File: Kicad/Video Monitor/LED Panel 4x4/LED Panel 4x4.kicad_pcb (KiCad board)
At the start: 2 copper layers, 20.1 x 20.1 mm, 34 parts, among them IC2 74VHC273FT, IC3 74VHC273FT

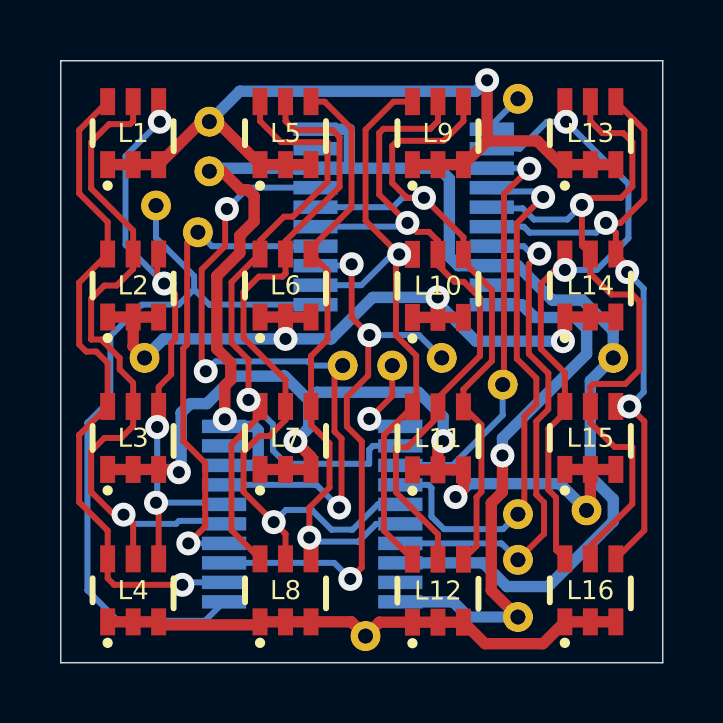
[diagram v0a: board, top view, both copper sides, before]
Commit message: LED Address attempted.
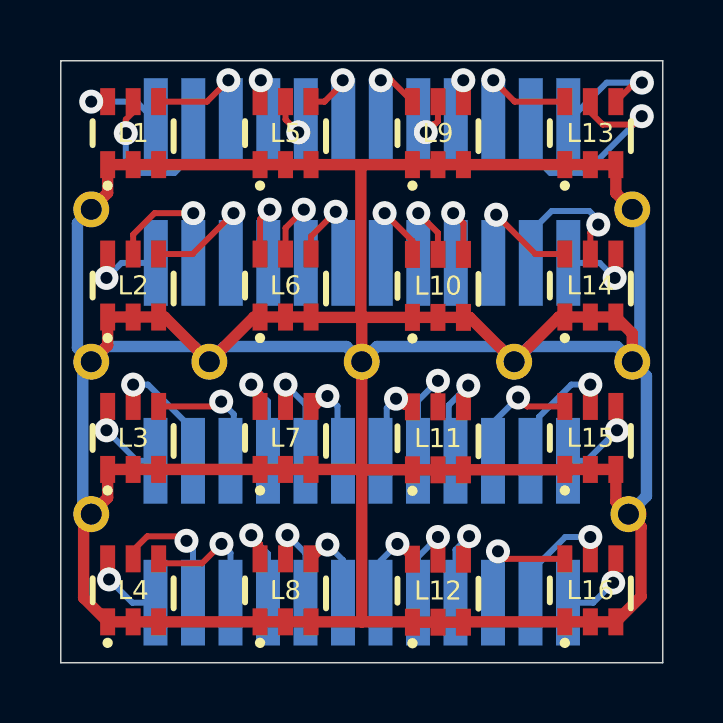
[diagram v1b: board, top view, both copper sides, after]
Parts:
- removed IC2, IC3: 74VHC273FT, SamacSys_Parts:SOP65P640X110-20N
- removed TP10, TP11, TP12, TP13, TP14, TP15, TP16: TestPoint, SamacSys_Parts:Point_D1.0mm_Drill0.5mm
- added J1: 504187-2470, SamacSys_Parts:5041872470, B.Cu at (125.3, 69.9)
- added J2: 504187-2470, SamacSys_Parts:5041872470, B.Cu at (125.3, 80.6)
- moved TP1 15.7 mm to (116.3, 75.2)
- moved TP3 14.4 mm to (116.3, 80.3)
- moved TP4 10.7 mm to (134.2, 80.3)
- moved TP9 8.76 mm to (130.3, 75.2)
- moved TP7 8.61 mm to (125.3, 75.2)
- moved TP6 8.05 mm to (134.3, 70.2)
- moved TP2 6.35 mm to (134.3, 75.2)
- moved TP8 6.10 mm to (120.2, 75.2)
- moved TP5 3.64 mm to (116.3, 70.2)
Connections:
- L1 pad C1: /G1 -> /GND
- L1 pad C2: /G1 -> /GND
- L1 pad C3: /G1 -> /GND
- L10 pad A1: /Q6 -> /Q18
- L10 pad A2: /Q7 -> /Q19
- L10 pad A3: /Q8 -> /Q20
- L10 pad C1: /G2 -> /GND
- L10 pad C2: /G2 -> /GND
- L10 pad C3: /G2 -> /GND
- L11 pad A1: /Q6 -> /Q30
- L11 pad A2: /Q7 -> /Q31
- L11 pad A3: /Q8 -> /Q32
- L11 pad C1: /G3 -> /GND
- L11 pad C2: /G3 -> /GND
- L11 pad C3: /G3 -> /GND
- L12 pad A1: /Q6 -> /Q42
- L12 pad A2: /Q7 -> /Q43
- L12 pad A3: /Q8 -> /Q44
- L12 pad C1: /G4 -> /GND
- L12 pad C2: /G4 -> /GND
- L12 pad C3: /G4 -> /GND
- L13 pad C1: /G1 -> /GND
- L13 pad C2: /G1 -> /GND
- L13 pad C3: /G1 -> /GND
- L14 pad A1: /Q9 -> /Q21
- L14 pad A2: /Q10 -> /Q22
- L14 pad A3: /Q11 -> /Q23
- L14 pad C1: /G2 -> /GND
- L14 pad C2: /G2 -> /GND
- L14 pad C3: /G2 -> /GND
- L15 pad A1: /Q9 -> /Q33
- L15 pad A2: /Q10 -> /Q34
- L15 pad A3: /Q11 -> /Q35
- L15 pad C1: /G3 -> /GND
- L15 pad C2: /G3 -> /GND
- L15 pad C3: /G3 -> /GND
- L16 pad A1: /Q9 -> /Q45
- L16 pad A2: /Q10 -> /Q46
- L16 pad A3: /Q11 -> /Q47
- L16 pad C1: /G4 -> /GND
- L16 pad C2: /G4 -> /GND
- L16 pad C3: /G4 -> /GND
- L2 pad A1: /Q0 -> /Q12
- L2 pad A2: /Q1 -> /Q13
- L2 pad A3: /Q2 -> /Q14
- L2 pad C1: /G2 -> /GND
- L2 pad C2: /G2 -> /GND
- L2 pad C3: /G2 -> /GND
- L3 pad A1: /Q0 -> /Q24
- L3 pad A2: /Q1 -> /Q25
- L3 pad A3: /Q2 -> /Q26
- L3 pad C1: /G3 -> /GND
- L3 pad C2: /G3 -> /GND
- L3 pad C3: /G3 -> /GND
- L4 pad A1: /Q0 -> /Q36
- L4 pad A2: /Q1 -> /Q37
- L4 pad A3: /Q2 -> /Q38
- L4 pad C1: /G4 -> /GND
- L4 pad C2: /G4 -> /GND
- L4 pad C3: /G4 -> /GND
- L5 pad C1: /G1 -> /GND
- L5 pad C2: /G1 -> /GND
- L5 pad C3: /G1 -> /GND
- L6 pad A1: /Q3 -> /Q15
- L6 pad A2: /Q4 -> /Q16
- L6 pad A3: /Q5 -> /Q17
- L6 pad C1: /G2 -> /GND
- L6 pad C2: /G2 -> /GND
- L6 pad C3: /G2 -> /GND
- L7 pad A1: /Q3 -> /Q27
- L7 pad A2: /Q4 -> /Q28
- L7 pad A3: /Q5 -> /Q29
- L7 pad C1: /G3 -> /GND
- L7 pad C2: /G3 -> /GND
- L7 pad C3: /G3 -> /GND
- L8 pad A1: /Q3 -> /Q39
- L8 pad A2: /Q4 -> /Q40
- L8 pad A3: /Q5 -> /Q41
- L8 pad C1: /G4 -> /GND
- L8 pad C2: /G4 -> /GND
- L8 pad C3: /G4 -> /GND
- L9 pad C1: /G1 -> /GND
- L9 pad C2: /G1 -> /GND
- L9 pad C3: /G1 -> /GND
- TP1 pad 1: /D5 -> /GND
- TP2 pad 1: /D4 -> /GND
- TP3 pad 1: /D3 -> /GND
- TP4 pad 1: /D2 -> /GND
- TP5 pad 1: /D1 -> /GND
- TP6 pad 1: /D0 -> /GND
- TP7 pad 1: /~{Reset} -> /GND
- TP8 pad 1: /~{Y0} -> /GND
- TP9 pad 1: /~{Y1} -> /GND
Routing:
- net /GND: track 49.8 -> 142.9 mm, vias 1 -> 0
- net /G3: track 31.3 -> 0.00 mm, vias 4 -> 0
- net /G1: track 26.7 -> 0.00 mm, vias 1 -> 0
- net /G2: track 26.0 -> 0.00 mm, vias 3 -> 0
- net /~{Reset}: track 25.0 -> 0.00 mm
- net /Q3: track 26.5 -> 1.83 mm
- net /Q4: track 25.5 -> 1.20 mm
- net /D2: track 22.6 -> 0.00 mm, vias 3 -> 0
- net /Q7: track 23.2 -> 1.21 mm
- net /Q8: track 23.3 -> 1.82 mm
- net /D0: track 19.8 -> 0.00 mm, vias 3 -> 0
- net /Q0: track 22.5 -> 2.97 mm
- net /Q1: track 23.5 -> 4.46 mm
- net /Q6: track 21.7 -> 2.71 mm
- net /3.3V: track 18.9 -> 0.00 mm, vias 1 -> 0
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
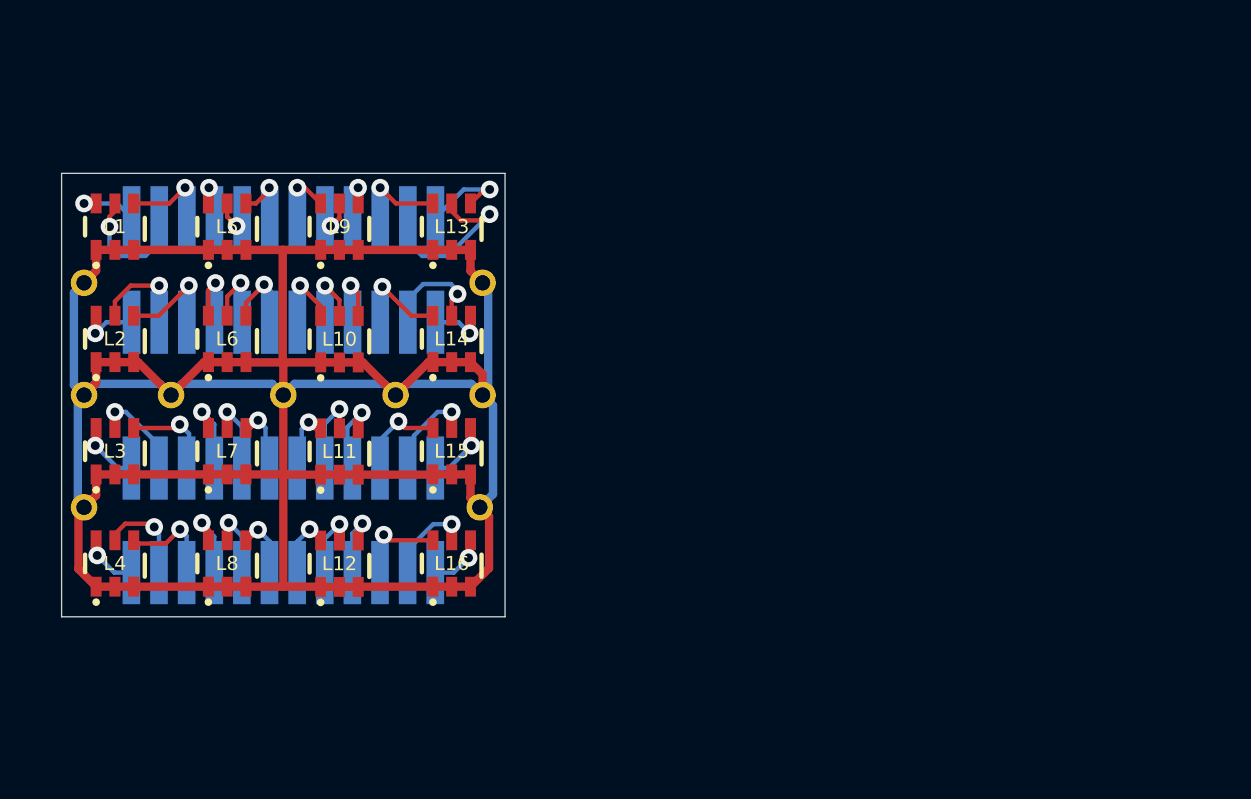
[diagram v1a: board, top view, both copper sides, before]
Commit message: Removed MPU copper fills.
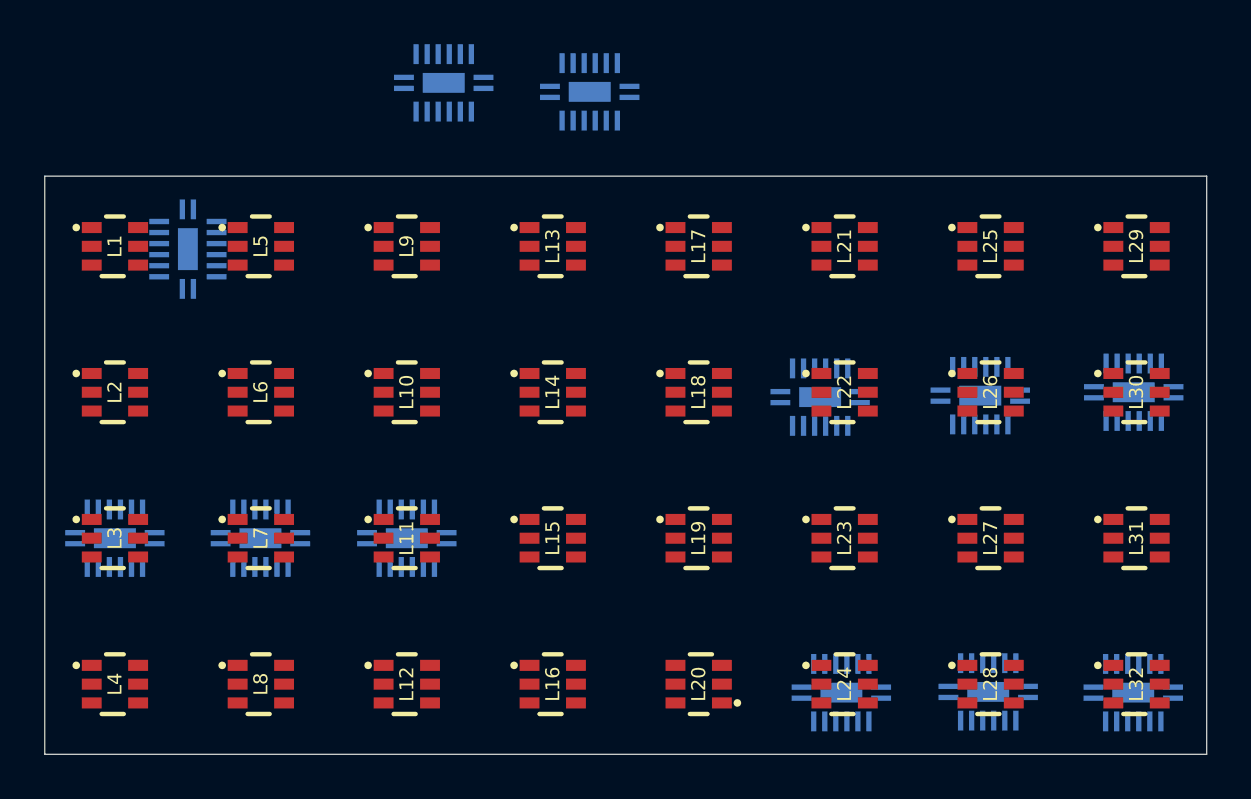
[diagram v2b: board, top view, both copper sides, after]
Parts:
- removed J1, J2: 504187-2470, SamacSys_Parts:5041872470
- removed TP1, TP2, TP3, TP4, TP5, TP6, TP7, TP8, TP9: TestPoint, SamacSys_Parts:Point_D1.0mm_Drill0.5mm
- added IC1: 74HCT259BQ,115, SamacSys_Parts:74HCT259BQ115, B.Cu at (120.9, 68.6)
- added IC10: 74HCT259BQ,115, SamacSys_Parts:74HCT259BQ115, B.Cu at (117.6, 81.7)
- added IC11: 74HCT259BQ,115, SamacSys_Parts:74HCT259BQ115, B.Cu at (130.9, 81.7)
- added IC12: 74HCT259BQ,115, SamacSys_Parts:74HCT259BQ115, B.Cu at (124.2, 81.7)
- added IC2: 74HCT259BQ,115, SamacSys_Parts:74HCT259BQ115, B.Cu at (132.5, 61.1)
- added IC3: 74HCT259BQ,115, SamacSys_Parts:74HCT259BQ115, B.Cu at (139.1, 61.5)
- added IC4: 74HCT259BQ,115, SamacSys_Parts:74HCT259BQ115, B.Cu at (156.8, 75.3)
- added IC5: 74HCT259BQ,115, SamacSys_Parts:74HCT259BQ115, B.Cu at (149.6, 75.3)
- added IC6: 74HCT259BQ,115, SamacSys_Parts:74HCT259BQ115, B.Cu at (163.7, 75.1)
- added IC7: 74HCT259BQ,115, SamacSys_Parts:74HCT259BQ115, B.Cu at (163.7, 88.7)
- added IC8: 74HCT259BQ,115, SamacSys_Parts:74HCT259BQ115, B.Cu at (150.5, 88.7)
- added IC9: 74HCT259BQ,115, SamacSys_Parts:74HCT259BQ115, B.Cu at (157.2, 88.7)
- added L17: KRTBLFLM71.32, SamacSys_Parts:KRTBLFLM7132TXUYEVVTAUDPRXTUKY, F.Cu at (144.1, 68.5)
- added L18: KRTBLFLM71.32, SamacSys_Parts:KRTBLFLM7132TXUYEVVTAUDPRXTUKY, F.Cu at (144.1, 75.1)
- added L19: KRTBLFLM71.32, SamacSys_Parts:KRTBLFLM7132TXUYEVVTAUDPRXTUKY, F.Cu at (144.1, 81.7)
- added L20: KRTBLFLM71.32, SamacSys_Parts:KRTBLFLM7132TXUYEVVTAUDPRXTUKY, F.Cu at (144.1, 88.3)
- added L21: KRTBLFLM71.32, SamacSys_Parts:KRTBLFLM7132TXUYEVVTAUDPRXTUKY, F.Cu at (150.7, 68.5)
- added L22: KRTBLFLM71.32, SamacSys_Parts:KRTBLFLM7132TXUYEVVTAUDPRXTUKY, F.Cu at (150.7, 75.1)
- added L23: KRTBLFLM71.32, SamacSys_Parts:KRTBLFLM7132TXUYEVVTAUDPRXTUKY, F.Cu at (150.7, 81.7)
- added L24: KRTBLFLM71.32, SamacSys_Parts:KRTBLFLM7132TXUYEVVTAUDPRXTUKY, F.Cu at (150.7, 88.3)
- added L25: KRTBLFLM71.32, SamacSys_Parts:KRTBLFLM7132TXUYEVVTAUDPRXTUKY, F.Cu at (157.3, 68.5)
- added L26: KRTBLFLM71.32, SamacSys_Parts:KRTBLFLM7132TXUYEVVTAUDPRXTUKY, F.Cu at (157.3, 75.1)
- added L27: KRTBLFLM71.32, SamacSys_Parts:KRTBLFLM7132TXUYEVVTAUDPRXTUKY, F.Cu at (157.3, 81.7)
- added L28: KRTBLFLM71.32, SamacSys_Parts:KRTBLFLM7132TXUYEVVTAUDPRXTUKY, F.Cu at (157.3, 88.3)
- added L29: KRTBLFLM71.32, SamacSys_Parts:KRTBLFLM7132TXUYEVVTAUDPRXTUKY, F.Cu at (163.9, 68.5)
- added L30: KRTBLFLM71.32, SamacSys_Parts:KRTBLFLM7132TXUYEVVTAUDPRXTUKY, F.Cu at (163.9, 75.1)
- added L31: KRTBLFLM71.32, SamacSys_Parts:KRTBLFLM7132TXUYEVVTAUDPRXTUKY, F.Cu at (163.9, 81.7)
- added L32: KRTBLFLM71.32, SamacSys_Parts:KRTBLFLM7132TXUYEVVTAUDPRXTUKY, F.Cu at (163.9, 88.3)
- moved L16 7.12 mm to (137.5, 88.3), turned to -90 degrees
- moved L12 6.24 mm to (130.9, 88.3), turned to -90 degrees
- moved L15 6.03 mm to (137.5, 81.7), turned to -90 degrees
- moved L8 5.67 mm to (124.3, 88.3), turned to -90 degrees
- moved L4 5.46 mm to (117.6, 88.3), turned to -90 degrees
- moved L14 5.17 mm to (137.5, 75.1), turned to -90 degrees
- moved L11 4.97 mm to (130.9, 81.7), turned to -90 degrees
- moved L13 4.66 mm to (137.5, 68.5), turned to -90 degrees
- moved L7 4.22 mm to (124.3, 81.7), turned to -90 degrees
- moved L3 3.94 mm to (117.6, 81.7), turned to -90 degrees
- moved L10 3.88 mm to (130.9, 75.1), turned to -90 degrees
- moved L9 3.18 mm to (130.9, 68.5), turned to -90 degrees
- moved L6 2.85 mm to (124.3, 75.1), turned to -90 degrees
- moved L2 2.41 mm to (117.6, 75.1), turned to -90 degrees
- moved L5 1.76 mm to (124.3, 68.5), turned to -90 degrees
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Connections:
- L1 pad A1: /Q0 -> /B0
- L1 pad A2: /Q1 -> /G0
- L1 pad A3: /Q2 -> /R0
- L10 pad A1: /Q18 -> /B10
- L10 pad A2: /Q19 -> /G10
- L10 pad A3: /Q20 -> /R10
- L11 pad A1: /Q30 -> /B18
- L11 pad A2: /Q31 -> /G18
- L11 pad A3: /Q32 -> /R18
- L12 pad A1: /Q42 -> /B26
- L12 pad A2: /Q43 -> /G26
- L12 pad A3: /Q44 -> /R26
- L13 pad A1: /Q9 -> /B3
- L13 pad A2: /Q10 -> /G3
- L13 pad A3: /Q11 -> /R3
- L14 pad A1: /Q21 -> /B11
- L14 pad A2: /Q22 -> /G11
- L14 pad A3: /Q23 -> /R11
- L15 pad A1: /Q33 -> /B19
- L15 pad A2: /Q34 -> /G19
- L15 pad A3: /Q35 -> /R19
- L16 pad A1: /Q45 -> /B27
- L16 pad A2: /Q46 -> /G27
- L16 pad A3: /Q47 -> /R27
- L2 pad A1: /Q12 -> /B8
- L2 pad A2: /Q13 -> /G8
- L2 pad A3: /Q14 -> /R8
- L3 pad A1: /Q24 -> /B16
- L3 pad A2: /Q25 -> /G16
- L3 pad A3: /Q26 -> /R16
- L4 pad A1: /Q36 -> /B24
- L4 pad A2: /Q37 -> /G24
- L4 pad A3: /Q38 -> /R24
- L5 pad A1: /Q3 -> /B1
- L5 pad A2: /Q4 -> /G1
- L5 pad A3: /Q5 -> /R1
- L6 pad A1: /Q15 -> /B9
- L6 pad A2: /Q16 -> /G9
- L6 pad A3: /Q17 -> /R9
- L7 pad A1: /Q27 -> /B17
- L7 pad A2: /Q28 -> /G17
- L7 pad A3: /Q29 -> /R17
- L8 pad A1: /Q39 -> /B25
- L8 pad A2: /Q40 -> /G25
- L8 pad A3: /Q41 -> /R25
- L9 pad A1: /Q6 -> /B2
- L9 pad A2: /Q7 -> /G2
- L9 pad A3: /Q8 -> /R2
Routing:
- net /GND: track 142.9 -> 0.00 mm
- net /Q10: track 6.75 -> 0.00 mm, vias 1 -> 0
- net /Q14: track 4.81 -> 0.00 mm, vias 1 -> 0
- net /Q27: track 4.63 -> 0.00 mm, vias 1 -> 0
- net /Q13: track 4.61 -> 0.00 mm, vias 1 -> 0
- net /Q1: track 4.46 -> 0.00 mm, vias 1 -> 0
- net /Q38: track 4.30 -> 0.00 mm, vias 1 -> 0
- net /Q26: track 4.19 -> 0.00 mm, vias 1 -> 0
- net /Q37: track 4.19 -> 0.00 mm, vias 1 -> 0
- net /Q11: track 4.12 -> 0.00 mm, vias 1 -> 0
- net /Q45: track 4.11 -> 0.00 mm, vias 1 -> 0
- net /Q31: track 4.09 -> 0.00 mm, vias 1 -> 0
- net /Q9: track 4.04 -> 0.00 mm, vias 1 -> 0
- net /Q5: track 3.86 -> 0.00 mm, vias 1 -> 0
- net /Q34: track 3.72 -> 0.00 mm, vias 1 -> 0
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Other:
- board size 20.1 x 20.1 mm -> 52.6 x 26.2 mm
